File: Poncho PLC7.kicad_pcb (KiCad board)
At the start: 2 copper layers, 135.6 x 83.3 mm, 99 parts, among them J1 TB_1X2-PonchoPLC-rescue, J10 Conn_02x12_Odd_Even, J13 Conn_02x05_Odd_Even, J18 Conn_02x05_Odd_Even, J2 TB_1X3-PonchoPLC-rescue, J3 TB_1X2, J4 TB_1X2, J5 TB_1X2, J6 TB_1X2, J7 Conn_02x12_Odd_Even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

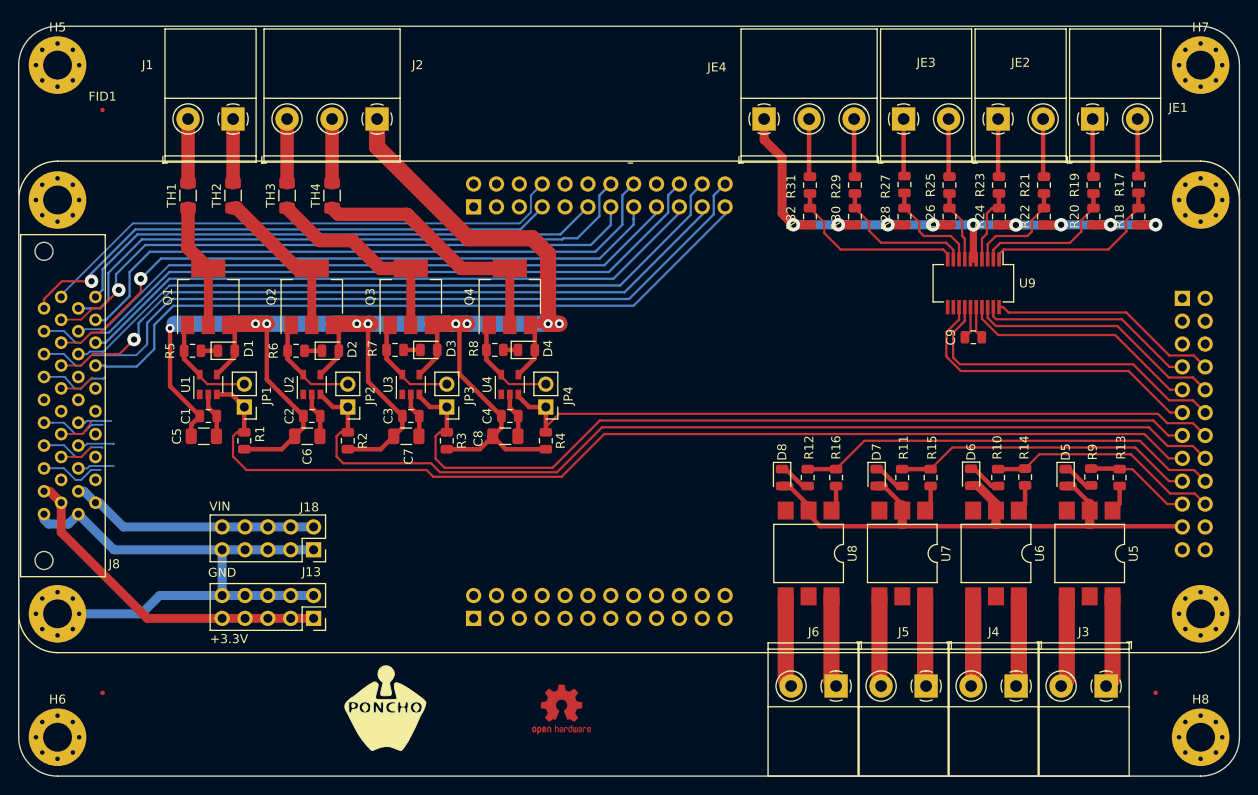
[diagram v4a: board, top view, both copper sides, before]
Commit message: Ruteo Casi terminado (faltan planos de masa)
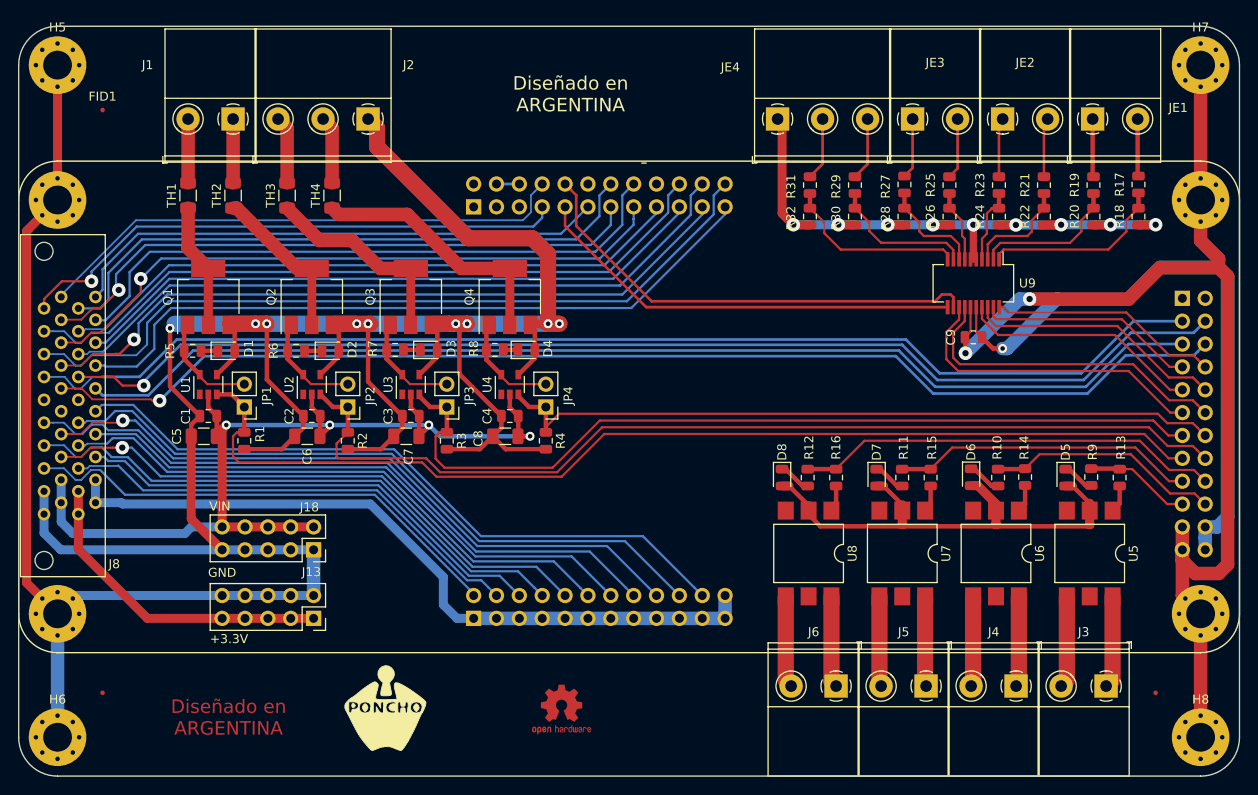
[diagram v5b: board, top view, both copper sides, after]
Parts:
- moved JE4 1.50 mm to (118.0, 71.0)
- moved J2 1.00 mm to (72.5, 71.0)
- moved JE3 1.00 mm to (133.0, 71.0)
- moved JE2 0.50 mm to (143.0, 71.0)
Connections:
- C1 pad 1: GND -> GNDPWR
- C2 pad 1: GND -> GNDPWR
- C3 pad 1: GND -> GNDPWR
- C4 pad 1: GND -> GNDPWR
- C5 pad 1: GND -> GNDPWR
- C6 pad 1: GND -> GNDPWR
- C7 pad 1: GND -> GNDPWR
- C8 pad 1: GND -> GNDPWR
- C9 pad 1: GND -> GNDS
- D1 pad 2: GND -> GNDPWR
- D2 pad 2: GND -> GNDPWR
- D3 pad 2: GND -> GNDPWR
- D4 pad 2: GND -> GNDPWR
- H1 pad 1: GND -> GNDPWR
- H2 pad 1: GND -> GNDPWR
- H3 pad 1: GND -> GNDS
- H4 pad 1: GND -> GNDS
- H5 pad 1: GND -> GNDPWR
- H6 pad 1: GND -> GNDPWR
- H7 pad 1: GND -> GNDS
- H8 pad 1: GND -> GNDS
- J10 pad 1: GND -> GNDA
- J10 pad 11: GND -> GNDA
- J10 pad 13: GND -> GNDA
- J10 pad 15: GND -> GNDA
- J10 pad 17: GND -> GNDA
- J10 pad 19: GND -> GNDA
- J10 pad 21: GND -> GNDA
- J10 pad 23: GND -> GNDA
- J10 pad 24: GND -> GNDA
- J10 pad 3: GND -> GNDA
- J10 pad 5: GND -> GNDA
- J10 pad 7: GND -> GNDA
- J10 pad 9: GND -> GNDA
- J13 pad 1: +3V3 -> +3.3VP
- J13 pad 10: GND -> GNDPWR
- J13 pad 2: GND -> GNDPWR
- J13 pad 3: +3V3 -> +3.3VP
- J13 pad 4: GND -> GNDPWR
- J13 pad 5: +3V3 -> +3.3VP
- J13 pad 6: GND -> GNDPWR
- J13 pad 7: +3V3 -> +3.3VP
- J13 pad 8: GND -> GNDPWR
- J13 pad 9: +3V3 -> +3.3VP
- J18 pad 1: GND -> GNDPWR
- J18 pad 3: GND -> GNDPWR
- J18 pad 5: GND -> GNDPWR
- J18 pad 7: GND -> GNDPWR
- J18 pad 9: GND -> GNDPWR
- J2 pad 1: GND -> GNDPWR
- J7 pad 21: GND -> GNDS
- J7 pad 23: GND -> GNDS
- J8 pad 1: GND -> GNDPWR
- J8 pad 11: +3V3 -> +5V
- J8 pad 12: Net-(J8-Pad12) -> +5V
- J8 pad 13: /BaseCIAA7/ADC3_INP1 -> /BaseCIAA7/ADC1_INP16
- J8 pad 14: /BaseCIAA7/ADC12_INP19 -> /BaseCIAA7/ADC12_INP3
- J8 pad 16: /BaseCIAA7/PC6 -> /BaseCIAA7/PC7
- J8 pad 2: +3V3 -> GNDPWR
- J8 pad 21: GND -> +3.3VP
- J8 pad 22: +5V -> +3.3VP
- J8 pad 23: /BaseCIAA7/PC13 -> /BaseCIAA7/ADC123_INP10
- J8 pad 24: /BaseCIAA7/ADC1_INP16 -> /BaseCIAA7/ADC12_INP15
- J8 pad 25: /BaseCIAA7/ADC12_INP3 -> /BaseCIAA7/ADC12_INP5
- J8 pad 3: /BaseCIAA7/ADC123_INP10 -> /BaseCIAA7/PC13
- J8 pad 31: +5V -> GNDA
- J8 pad 32: Net-(J8-Pad32) -> GNDA
- J8 pad 36: /BaseCIAA7/PC7 -> /BaseCIAA7/PC6
- J8 pad 4: /BaseCIAA7/ADC12_INP15 -> /BaseCIAA7/ADC3_INP1
- J8 pad 5: /BaseCIAA7/ADC12_INP5 -> /BaseCIAA7/ADC12_INP19
- J9 pad 1: GND -> Net-(J9-Pad1)
- J9 pad 2: GND -> Net-(J9-Pad2)
- J9 pad 4: +3V3 -> Net-(J9-Pad4)
- J9 pad 6: +3V3 -> Net-(J9-Pad4)
- Q1 pad 3: GND -> GNDPWR
- Q2 pad 3: GND -> GNDPWR
- Q3 pad 3: GND -> GNDPWR
- Q4 pad 3: GND -> GNDPWR
- R1 pad 2: GND -> GNDPWR
- R2 pad 2: GND -> GNDPWR
- R3 pad 2: GND -> GNDPWR
- R4 pad 2: GND -> GNDPWR
- U1 pad 4: GND -> GNDPWR
- U2 pad 4: GND -> GNDPWR
- U3 pad 4: GND -> GNDPWR
- U4 pad 4: GND -> GNDPWR
- U9 pad 15: GND -> GNDS
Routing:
- net GNDPWR: track 0.00 -> 363.9 mm, vias 0 -> 9
- net GND: track 338.1 -> 55.0 mm, vias 9 -> 0
- net /BaseCIAA7/PC7: track 0.00 -> 133.7 mm, vias 0 -> 1
- net /BaseCIAA7/PA8: track 0.00 -> 131.7 mm, vias 0 -> 1
- net GNDS: track 0.00 -> 125.8 mm, vias 0 -> 2
- net /BaseCIAA7/PC9: track 7.94 -> 133.3 mm
- net /BaseCIAA7/PC6: track 3.94 -> 126.8 mm
- net GNDA: track 0.00 -> 82.2 mm
- net /BaseCIAA7/ADC12_INN5_INP9: track 0.00 -> 76.5 mm
- net /BaseCIAA7/ADC12_INP3: track 3.74 -> 74.8 mm, vias 0 -> 1
- net /BaseCIAA7/ADC12_INP19: track 4.01 -> 74.3 mm
- net /BaseCIAA7/ADC12_INP5: track 7.47 -> 75.8 mm
- net /BaseCIAA7/ADC12_INP18: track 0.00 -> 64.7 mm
- net /BaseCIAA7/ADC3_INP1: track 3.80 -> 63.2 mm
- net /BaseCIAA7/ADC1_INP16: track 4.04 -> 63.3 mm, vias 0 -> 1
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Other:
- board text added: "Diseñado en ARGENTINA"
